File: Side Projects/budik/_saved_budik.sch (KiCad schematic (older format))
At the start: 73 parts, among them J1 Conn_01x02_Male, J2 USB_OTG, J3 FTDI, Q1 BSS138, SW1 SW_DPST_x2, SW2 SW_DPST_x2, SW3 SW_SPDT, U1 ESP-12, U2 MCP23018-E_SP, U3 uA7805, U4 LD1117S33CTR

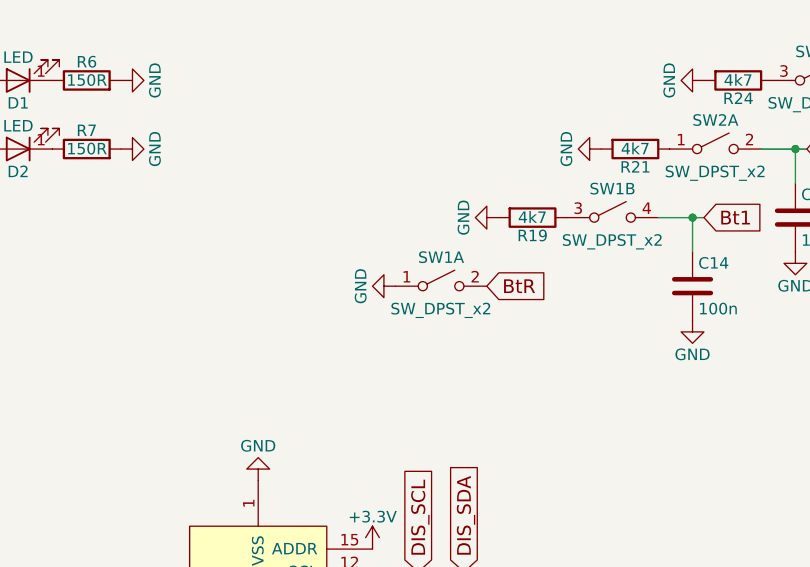
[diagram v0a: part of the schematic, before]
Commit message: Add some pcb parts
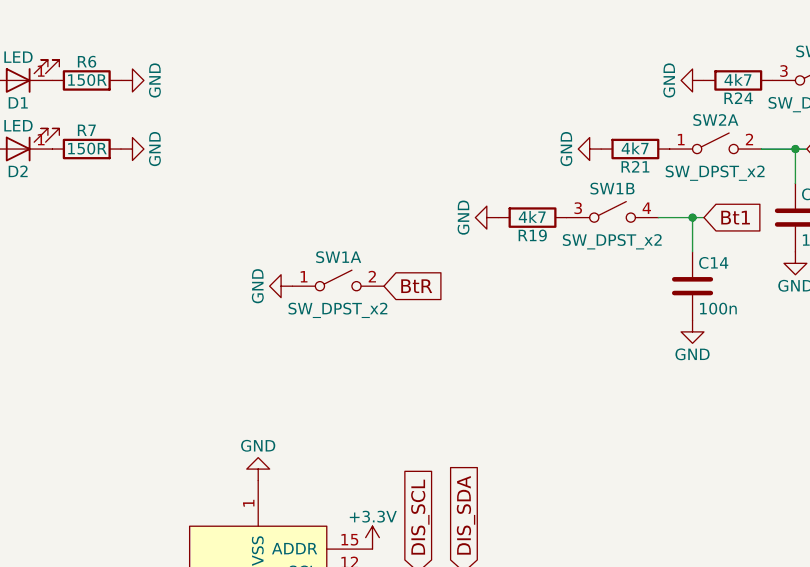
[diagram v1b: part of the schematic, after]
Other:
- moved on the sheet: SW1A
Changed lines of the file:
@@
 Text GLabel 2050 5400 2    60   Input ~ 0
 BtR
-Text GLabel 4700 4150 2    60   Input ~ 0
+Text GLabel 4250 4150 2    60   Input ~ 0
 BtR
 $Comp
 L SW_DPST_x2-RESCUE-budik SW1
 U 1 1 5B003A6B
-P 4500 4150
-F 0 "SW1" H 4500 4275 50  0000 C CNN
-F 1 "SW_DPST_x2" H 4500 4050 50  0000 C CNN
-F 2 "Buttons_Switches_THT:SW_PUSH_6mm" H 4500 4150 50  0001 C CNN
-F 3 "" H 4500 4150 50  0001 C CNN
-	1    4500 4150
+P 4050 4150
+F 0 "SW1" H 4050 4275 50  0000 C CNN
+F 1 "SW_DPST_x2" H 4050 4050 50  0000 C CNN
+F 2 "Buttons_Switches_THT:SW_PUSH_6mm" H 4050 4150 50  0001 C CNN
+F 3 "" H 4050 4150 50  0001 C CNN
+	1    4050 4150
 	1    0    0    -1
 $EndComp
@@
 L GND #PWR048
 U 1 1 5B003EF5
-P 4300 4150
-F 0 "#PWR048" H 4300 3900 50  0001 C CNN
-F 1 "GND" H 4300 4000 50  0000 C CNN
-F 2 "" H 4300 4150 50  0001 C CNN
-F 3 "" H 4300 4150 50  0001 C CNN
-	1    4300 4150
+P 3850 4150
+F 0 "#PWR048" H 3850 3900 50  0001 C CNN
+F 1 "GND" H 3850 4000 50  0000 C CNN
+F 2 "" H 3850 4150 50  0001 C CNN
+F 3 "" H 3850 4150 50  0001 C CNN
+	1    3850 4150
 	0    1    1    0
 $EndComp
